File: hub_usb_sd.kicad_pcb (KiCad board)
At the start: 4 copper layers, 50 x 50 mm, 66 parts, among them J1 Downstream_2, J2 Downstream_3, J3 I²C, J4 Upstream, J5 SD_Card, J6 EEPROM_Pgm, J7 External_Power, U1 USB2642-I_ML, U2 TPS2052C, U3 AT24CS04BN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

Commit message: Improved ground plane under U2 and corrected the positioning of C32-34
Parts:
- moved C32 29.7 mm to (149.8, 116.5), turned to 90 degrees
- moved C34 29.7 mm to (166.5, 91.9), turned to 180 degrees
- renumbered C34 to C32, C32 to C34

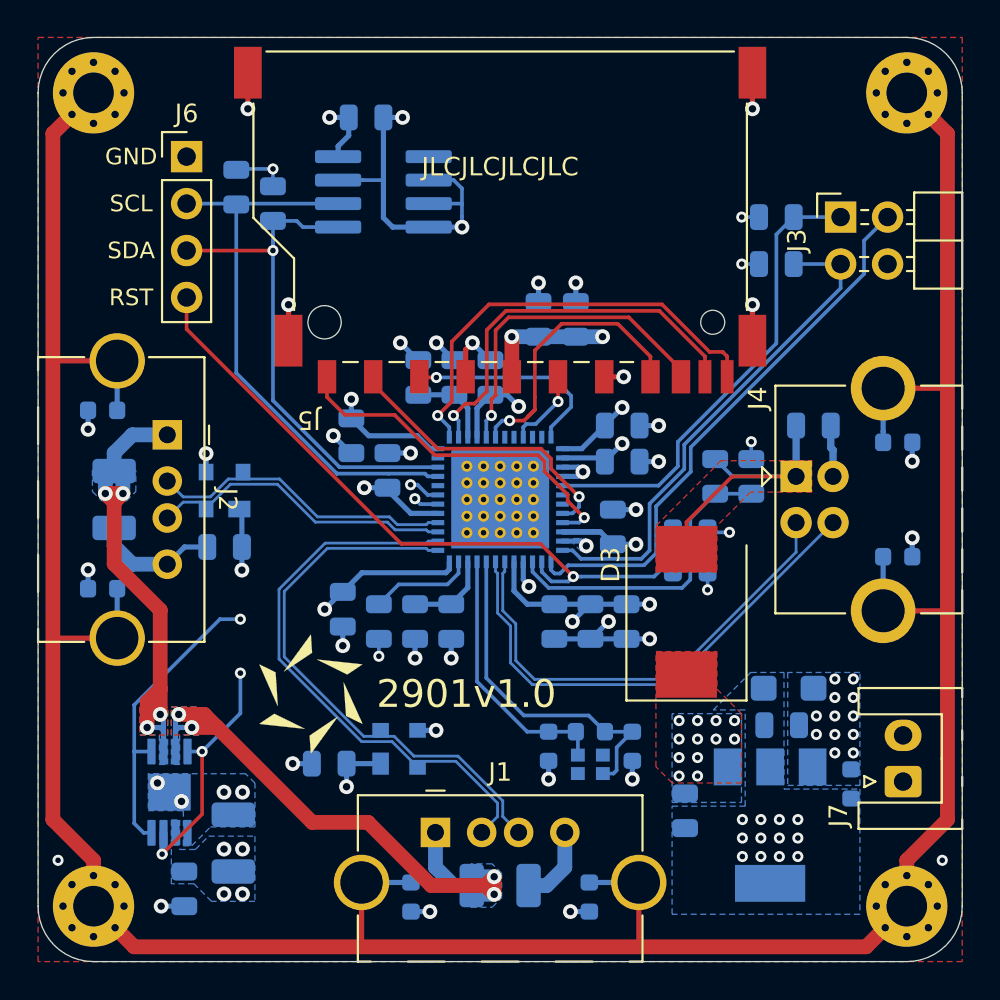
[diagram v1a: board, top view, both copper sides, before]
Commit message: Updated board layout to accommodate new power supply connector
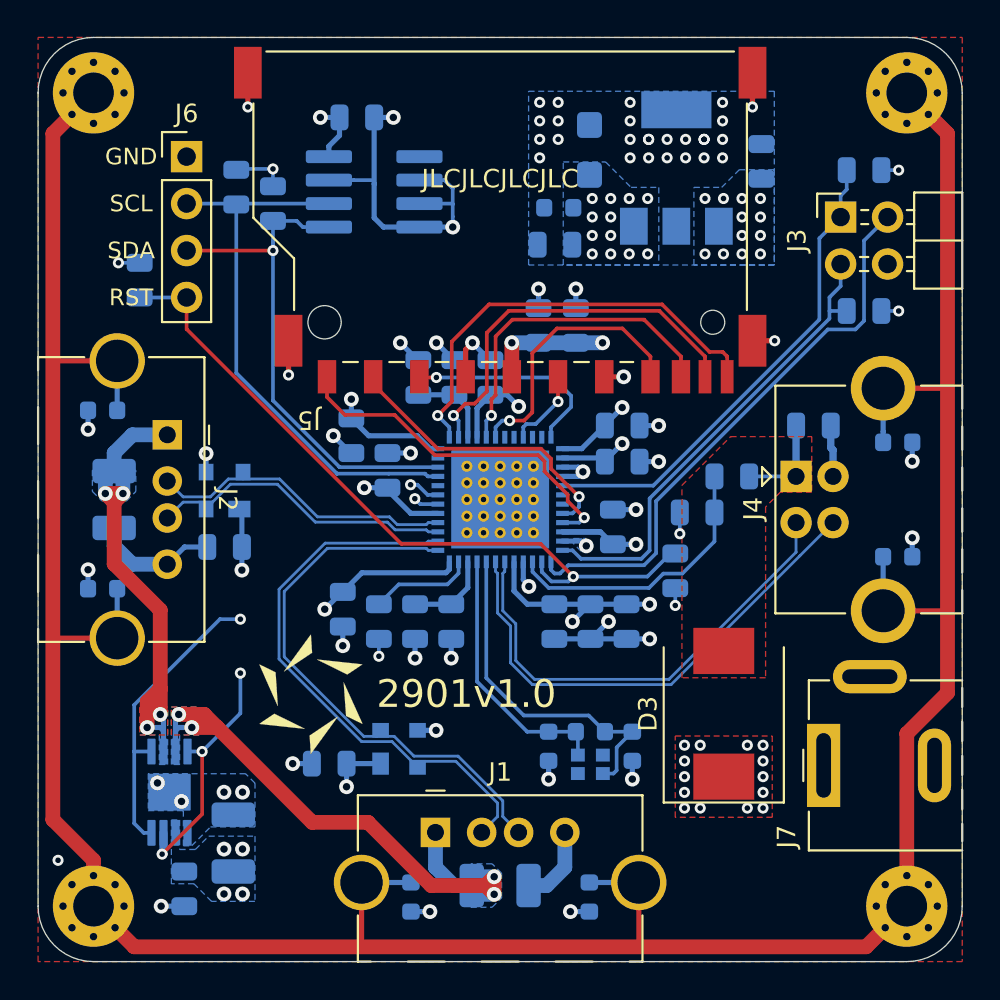
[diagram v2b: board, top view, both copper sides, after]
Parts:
- J7: footprint Extra:Metaltex_PEMN1-02_protruded_6_mm -> Extra:BarrelJack_DC-005_protruded_6_mm
- moved U4 35.9 mm to (154.5, 77.1), turned to 90 degrees
- moved C28 35.4 mm to (159.1, 76.7), turned to 270 degrees
- moved C30 35.0 mm to (148.2, 79.2), turned to 0 degrees
- moved R1 32.8 mm to (125.5, 83.1), turned to 270 degrees
- moved C31 31.1 mm to (149.8, 76.1), turned to 90 degrees
- moved C29 28.7 mm to (148.0, 81.2)
- moved D3 5.88 mm to (157.1, 106.6)
- moved R2 5.38 mm to (164.7, 84.8), turned to 180 degrees
- moved R3 5.38 mm to (164.7, 77.2), turned to 180 degrees
- moved J7 4.39 mm to (162.5, 109.4)
- moved R6 3.52 mm to (155.7, 95.7), turned to 180 degrees
- moved R5 0.90 mm to (157.5, 93.8), turned to 180 degrees
- moved C18 0.82 mm to (154.5, 98.9), turned to 90 degrees
- moved C27 0.50 mm to (137.2, 74.3)
- moved U3 0.50 mm to (138.2, 78.4)
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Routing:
- net Net-(C22-Pad2): track 15.9 -> 5.29 mm
- net Net-(J3-Pad3): track 27.4 -> 25.8 mm
- net Net-(R5-Pad2): track 16.8 -> 15.3 mm
- net GND: track 84.9 -> 83.9 mm, vias 57 -> 69
- net /nRESET: track 38.3 -> 39.3 mm
- net Net-(J3-Pad1): track 25.3 -> 26.3 mm
- net Net-(J3-Pad2): track 30.0 -> 30.9 mm
- net +3V3: track 59.1 -> 58.3 mm
- net Net-(J5-Pad7): track 15.5 -> 14.7 mm
- net Net-(C25-Pad2): track 20.1 -> 19.5 mm
- net +5V: vias 18 -> 32
